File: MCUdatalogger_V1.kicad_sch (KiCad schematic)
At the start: 25 parts, among them U1 24LC1025, U2 DS1337S+, U3 24LC1025, U4 ATMEGA328P-AU, Y1 Crystal

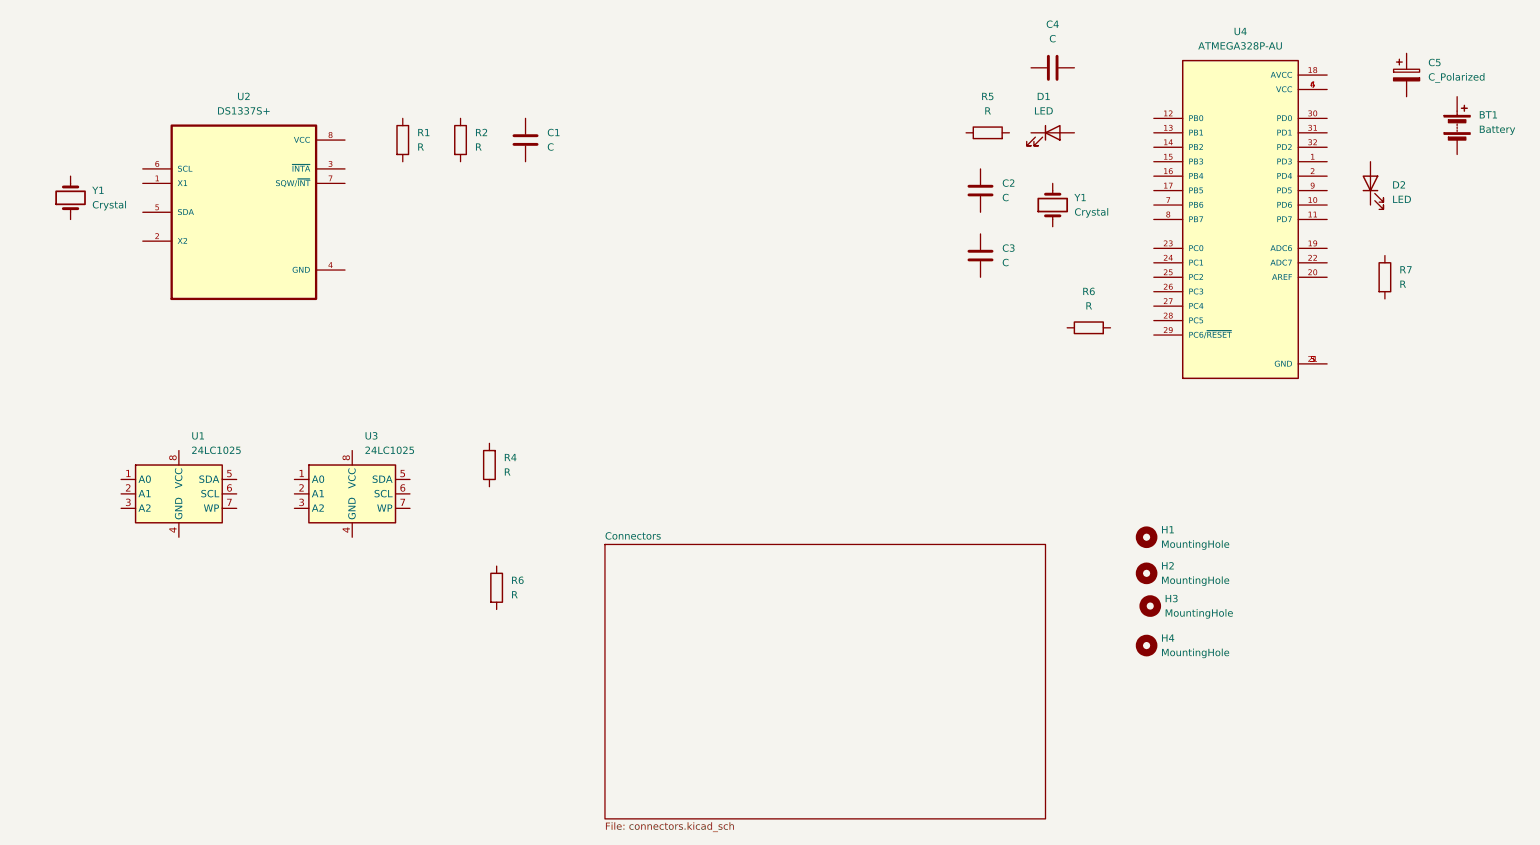
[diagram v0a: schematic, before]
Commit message: Complete wiring in the second sheet
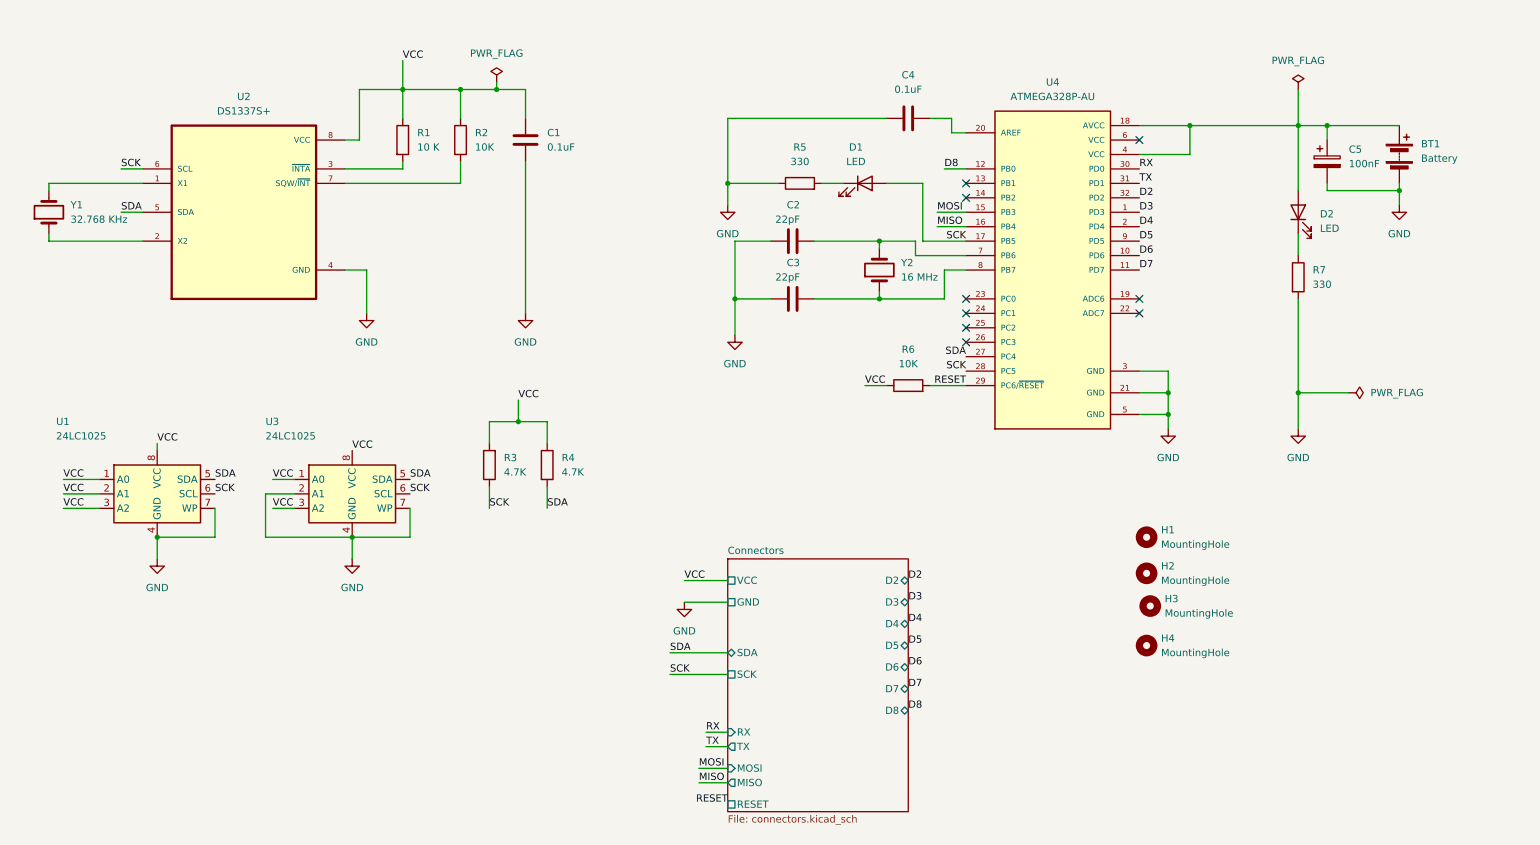
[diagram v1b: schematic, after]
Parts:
- BT1: footprint (none) -> Connector_PinHeader_2.54mm:PinHeader_1x02_P2.54mm_Vertical
- C1, C4: value C -> 0.1uF; footprint (none) -> Capacitor_SMD:C_0805_2012Metric
- C2, C3: value C -> 22pF; footprint (none) -> Capacitor_SMD:C_0805_2012Metric
- C5: value C_Polarized -> 100nF; footprint (none) -> Capacitor_SMD:C_0805_2012Metric
- D1, D2: footprint (none) -> LED_SMD:LED_0805_2012Metric
- H1, H2, H3, H4: footprint (none) -> MountingHole:MountingHole_2.1mm
- R1: value R -> 10 K; footprint (none) -> Resistor_SMD:R_0805_2012Metric
- R2, R6: value R -> 10K; footprint (none) -> Resistor_SMD:R_0805_2012Metric
- R3: renamed from R4; value R -> 4.7K; footprint (none) -> Resistor_SMD:R_0805_2012Metric
- R4: renamed from R6; value R -> 4.7K; footprint (none) -> Resistor_SMD:R_0805_2012Metric
- R5, R7: value R -> 330; footprint (none) -> Resistor_SMD:R_0805_2012Metric
- U1, U3: footprint (none) -> Package_SO:SOIC-8_5.23x5.23mm_P1.27mm
- U2: footprint SOIC127P600X175-8N -> Footprints:SOIC127P600X175-8N
- U4: footprint QFP80P900X900X120-32N -> Footprints:QFP80P900X900X120-32N
- Y1: value Crystal -> 32.768 KHz; footprint (none) -> Crystal:Crystal_SMD_5032-2Pin_5.0x3.2mm_HandSoldering
- Y2: renamed from Y1; value Crystal -> 16 MHz; footprint (none) -> Crystal:Crystal_SMD_5032-2Pin_5.0x3.2mm_HandSoldering
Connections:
- net GND: now reaches C3.1
- net GND: now also BT1.2 (-), C1.2, C2.1, C4.1, C5.2, R5.1, R7.2, U1.4 (GND), U1.7 (WP), U2.4 (GND), U3.2 (A1), U3.4 (GND), U3.7 (WP), U4.21 (GND), U4.3 (GND), U4.5 (GND)
- net at C3.2: now also U4.8 (PB7), Y2.1
- net at U2.1 (X1): now also Y1.2
- net at U2.2 (X2): now also Y1.1
- net at U2.3 (~{INTA}): now also R1.2
- net SDA: now reaches U2.5 (SDA)
- net SDA: now also R4.2, U1.5 (SDA), U3.5 (SDA), U4.27 (PC4)
- net SCK: now reaches U2.6 (SCL)
- net SCK: now also D1.2 (A), R3.1, U1.6 (SCL), U3.6 (SCL), U4.17 (PB5), U4.28 (PC5)
- net at U2.7 (SQW/~{INT}): now also R2.2
- net VCC: now reaches U2.8 (VCC)
- net VCC: now also C1.1, R1.1, R2.1, R3.2, R4.1, R6.1, U1.1 (A0), U1.2 (A1), U1.3 (A2), U1.8 (VCC), U3.1 (A0), U3.3 (A2), U3.8 (VCC)
- net at C4.2: now also U4.20 (AREF)
- net RESET: now reaches R6.2
- net RESET: now also U4.29 (PC6/~{RESET})
- net at R5.2: now also D1.1 (K)
- net at C2.2: now also U4.7 (PB6), Y2.2
- net at D2.1 (K): now also R7.1
- net at D2.2 (A): now also BT1.1 (+), C5.1, U4.18 (AVCC), U4.4 (VCC)
- net D3: now reaches U4.1 (PD3)
- net D6: now reaches U4.10 (PD6)
- net D7: now reaches U4.11 (PD7)
- net D8: now reaches U4.12 (PB0)
- net MOSI: now reaches U4.15 (PB3)
- net MISO: now reaches U4.16 (PB4)
- net D4: now reaches U4.2 (PD4)
- net RX: now reaches U4.30 (PD0)
- net TX: now reaches U4.31 (PD1)
- net D2: now reaches U4.32 (PD2)
- net at U4.6 (VCC): no longer U4.4 (VCC)
- net D5: now reaches U4.9 (PD5)
- no-connect marks 0 -> 9
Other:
- sheet Connectors ports: added D2, D3, D4, D5, D6, D7, D8, GND, MISO, MOSI, RESET, RX, SCK, SDA, TX, VCC; removed none
- moved on the sheet: BT1, C2, C3, C4, C5, D1, D2, R4, R5, R6, R7, U1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

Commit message: Completed comments.
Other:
- note added: "EEPROM"
- note added: "MCU"
- note added: "Mounting"
- note added: "Real time clock"
- moved on the sheet: H1, H2, H3, H4, R3, R4, U1, U3

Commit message: PCB Ready
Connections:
- net VCC: now also BT1.1 (+), C5.1, D2.2 (A), U4.18 (AVCC), U4.4 (VCC)
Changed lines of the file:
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@@
+    (effects (font (size 1.27 1.27)) (justify left bottom))
+  )
+  (label "VCC" (at 256.54 36.83 0) (fields_autoplaced)
     (effects (font (size 1.27 1.27)) (justify left bottom))
   )
